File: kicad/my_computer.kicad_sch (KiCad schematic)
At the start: 15 parts, among them SW1 SW_SPST

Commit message: update schematic
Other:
- added sheet RAM (RAM.kicad_sch)
- moved on the sheet: R1
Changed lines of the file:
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@@
+	(wire
+		(pts
+			(xy 226.06 73.66) (xy 226.06 72.39)
+		)
+		(stroke
+			(width 0)
+			(type default)
+		)
+	)
 	(wire
 		(pts
@@
 	(wire
 		(pts
-			(xy 226.06 80.01) (xy 226.06 83.82)
+			(xy 226.06 81.28) (xy 226.06 83.82)
 		)
 		(stroke
@@
 	(symbol
 		(lib_id "Device:R")
-		(at 226.06 76.2 0)
+		(at 226.06 77.47 0)
 		(unit 1)
 		(exclude_from_sim no)
@@
 		(fields_autoplaced yes)
 		(property "Reference" "R1"
-			(at 228.6 74.9299 0)
+			(at 228.6 76.1999 0)
 			(effects
 				(font
@@
 		)
 		(property "Value" "10k"
-			(at 228.6 77.4699 0)
-			(effects
-				(font
-					(size 1.27 1.27)
-				)
-				(justify left)
-			)
-		)
-		(property "Footprint" ""
-			(at 224.282 76.2 90)
+			(at 228.6 78.7399 0)
+			(effects
+				(font
+					(size 1.27 1.27)
+				)
+				(justify left)
+			)
+		)
+		(property "Footprint" ""
+			(at 224.282 77.47 90)
 			(effects
 				(font
@@
 		)
 		(property "Datasheet" "~"
-			(at 226.06 76.2 0)
+			(at 226.06 77.47 0)
 			(effects
 				(font
@@
 		)
 		(property "Description" "Resistor"
-			(at 226.06 76.2 0)
+			(at 226.06 77.47 0)
 			(effects
 				(font
@@
 				)
 			)
+		)
+	)
+	(sheet
+		(at 554.99 86.36)
+		(size 224.79 147.32)
+		(exclude_from_sim no)
+		(in_bom yes)
+		(on_board yes)
+		(dnp no)
+		(fields_autoplaced yes)
+		(stroke
+			(width 0.1524)
+			(type solid)
+		)
+		(fill
+			(color 0 0 0 0.0000)
+		)
+		(property "Sheetname" "RAM"
+			(at 554.99 85.6484 0)
+			(effects
+				(font
+					(size 1.27 1.27)
+				)
+				(justify left bottom)
+			)
+		)
+		(property "Sheetfile" "RAM.kicad_sch"
+			(at 554.99 234.2646 0)
+			(effects
+				(font
+					(size 1.27 1.27)
+				)
+				(justify left top)
+			)
+		)
+		(instances
+			(project "my_computer"
+				(path "/d90612be-a4bb-4b59-8bc6-93e31ea1f515"
+					(page "4")
+				)
+			)

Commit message: update schematic
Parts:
- removed 555_TIMER: LMC555CMX_NOPB, LMC555CMX_NOPB:SOIC127P599X175-8N, symbol LMC555CMX_NOPB:LMC555CMX_NOPB
- removed C3: 0.01uF, symbol Device:C
- removed C4: 1uF, symbol Device:C
- added C11: 0.01uF, symbol Device:C
- added C12: 1uF, symbol Device:C
- added CLK: LMC555CMX_NOPB, LMC555CMX_NOPB:SOIC127P599X175-8N, symbol LMC555CMX_NOPB:LMC555CMX_NOPB
- added R11, R12, R13, R32, R4, R5, R6, R7, R8: 10k, symbol Device:R
- added R30: 1k, symbol Device:R
- added R31: 100k, symbol Device:R
- added SW10, SW11, SW12, SW13, SW14, SW2, SW3, SW4, SW5, SW6, SW9: SW_SPST, symbol Switch:SW_SPST
- R2: value 1k -> 10k
- R3: value 100k -> 10k
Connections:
- net +3.3V: now also R3.1, CLK.8 (V+), R11.1, R12.1, R13.1, R30.1, R32.1, R4.1, R5.1, R6.1, R7.1, R8.1
- net CLK_RST: now also CLK.4 (~{RESET})
- net GND: now also C11.1, C12.2, SW10.1 (A), SW11.1 (A), SW12.1 (A), SW13.1 (A), SW14.1 (A), SW2.1 (A), SW3.1 (A), SW4.1 (A), SW5.1 (A), SW6.1 (A), SW9.1 (A)
- net WE_RAM: now reaches R3.2
- net WE_RAM: now also SW13.2 (B)
- net CE_RAM: now reaches R2.2
- net CE_RAM: now also SW12.2 (B); no longer R3.1
- new net: CLK.7 (DISCHARGE), R30.2, R31.1
- new net: C12.1, CLK.2 (~{TRIGGER}), CLK.6 (THRESHOLD), R31.2
- new net: C11.2, CLK.5 (CONTROL_VOLTAGE)
- new net CLR: R13.2, SW11.2 (B)
- new net LD_A: R11.2, SW9.2 (B)
- new net LD_B: R8.2, SW6.2 (B)
- new net LD_X: R4.2, SW2.2 (B)
- new net LD_Y: R6.2, SW4.2 (B)
- new net OE_A: R12.2, SW10.2 (B)
- new net OE_RAM: R32.2, SW14.2 (B)
- new net OE_X: R5.2, SW3.2 (B)
- new net OE_Y: R7.2, SW5.2 (B)
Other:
- added sheet ALU_REGS (ALU_REGS.kicad_sch)
- moved on the sheet: R1, SW1

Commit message: add PC
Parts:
- added R10, R34, R9: 10k, symbol Device:R
- added SW15, SW7, SW8: SW_SPST, symbol Switch:SW_SPST
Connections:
- net +3.3V: now also R34.1, R9.1, SW8.2 (B)
- net GND: now also R10.2, SW15.1 (A), SW7.1 (A)
- new net CLR_PC: R10.1, SW8.1 (A)
- new net INC_PC: R34.2, SW15.2 (B)
- new net LD_PC: R9.2, SW7.2 (B)
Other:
- added sheet Control Unit (CTRL_UNIT.kicad_sch)

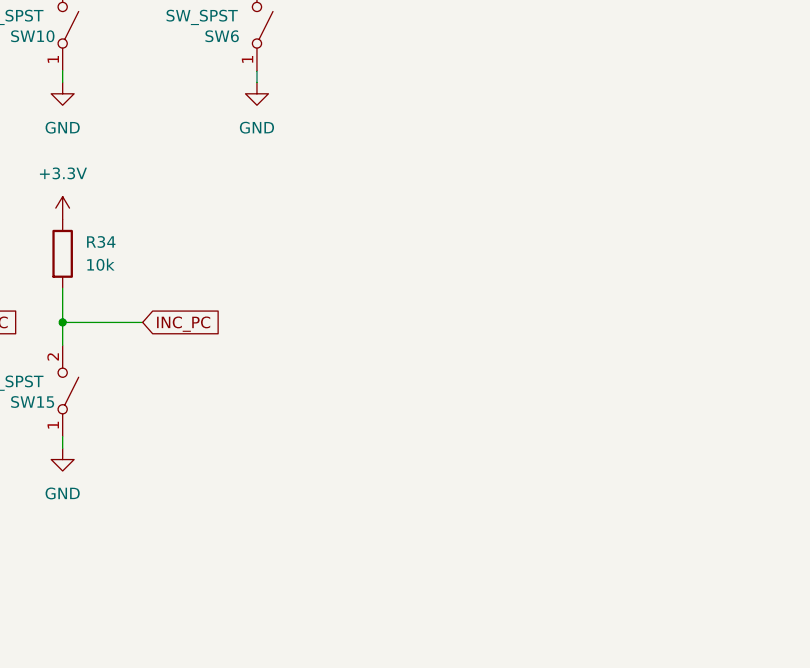
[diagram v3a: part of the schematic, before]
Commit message: update schematic
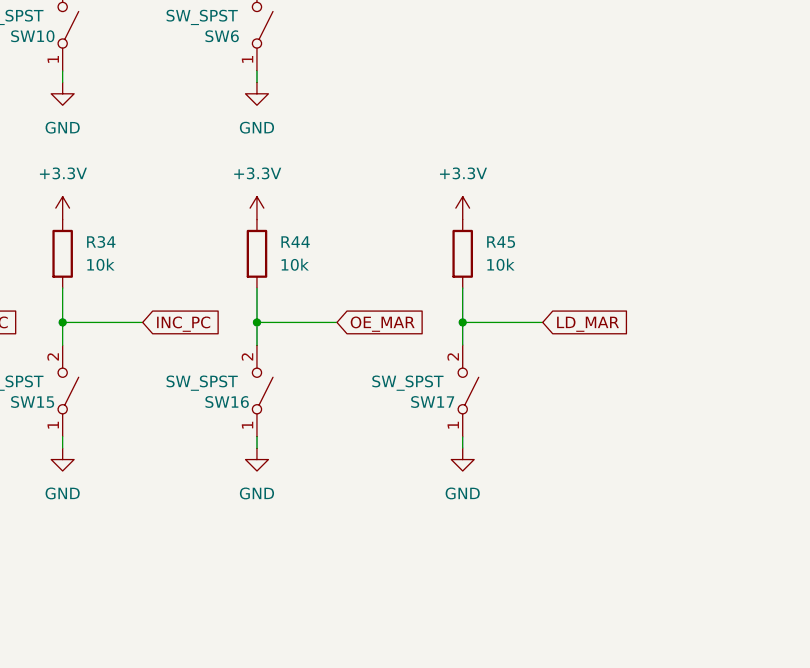
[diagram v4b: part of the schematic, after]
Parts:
- added R44, R45: 10k, symbol Device:R
- added SW16, SW17: SW_SPST, symbol Switch:SW_SPST
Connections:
- net +3.3V: now also R44.1, R45.1
- net GND: now also SW16.1 (A), SW17.1 (A)
- new net LD_MAR: R45.2, SW17.2 (B)
- new net OE_MAR: R44.2, SW16.2 (B)

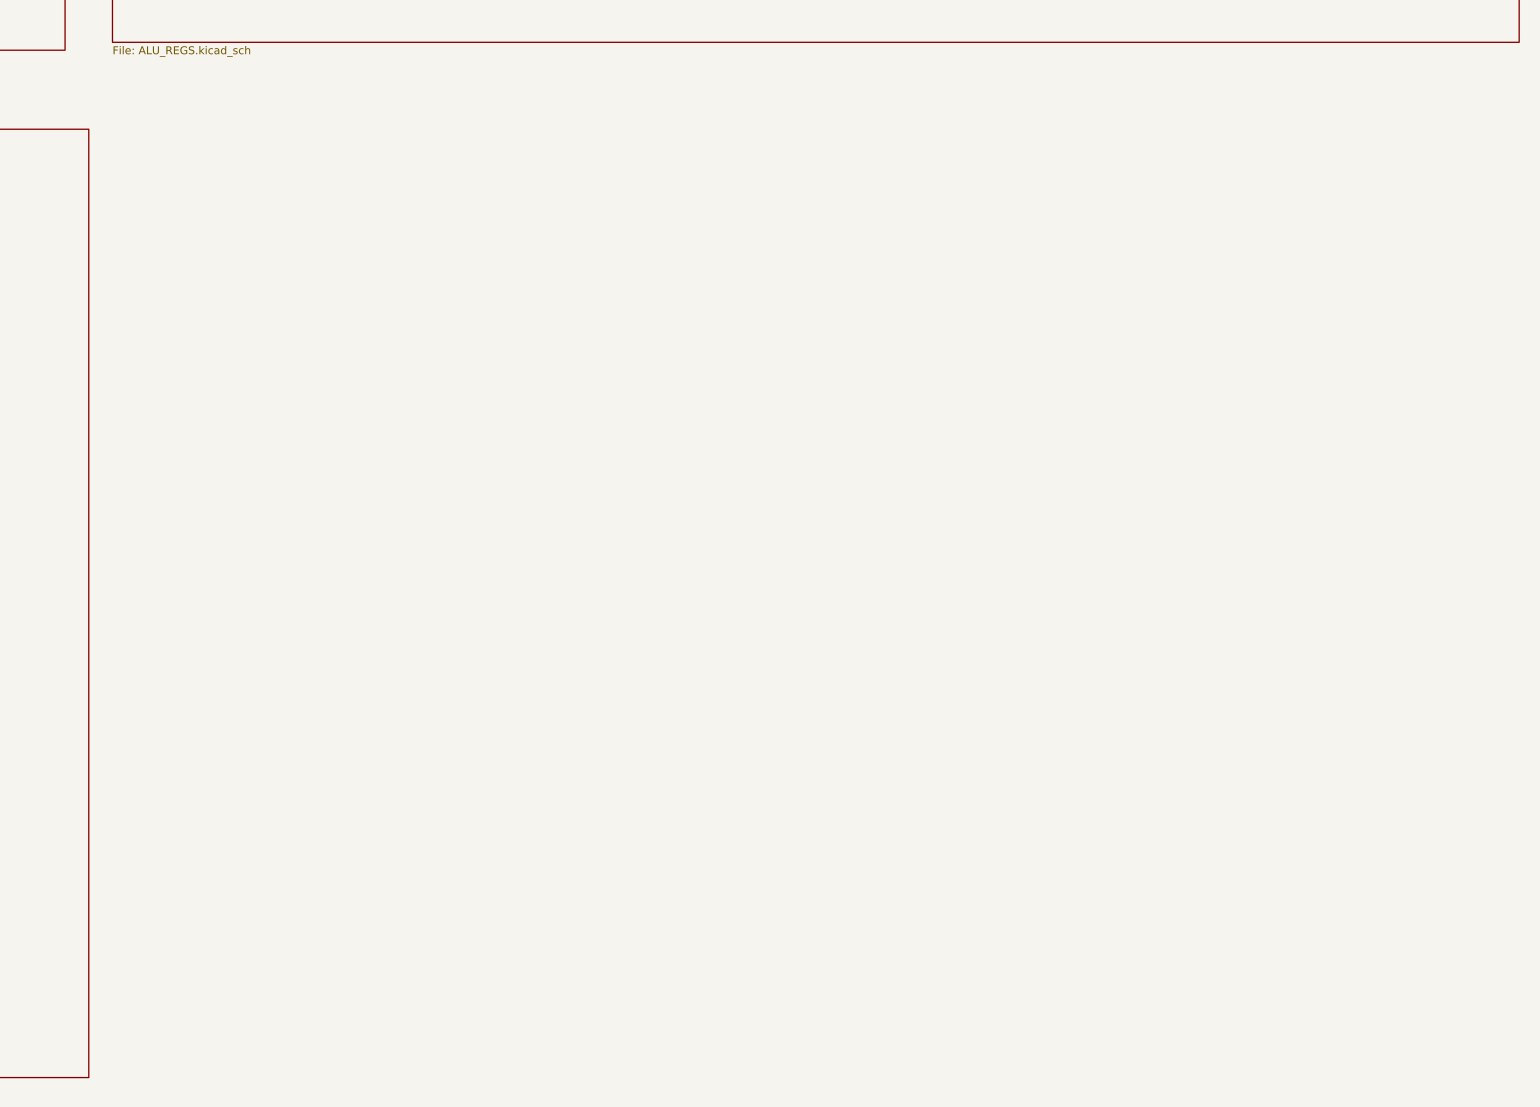
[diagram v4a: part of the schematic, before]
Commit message: add instruction decoder
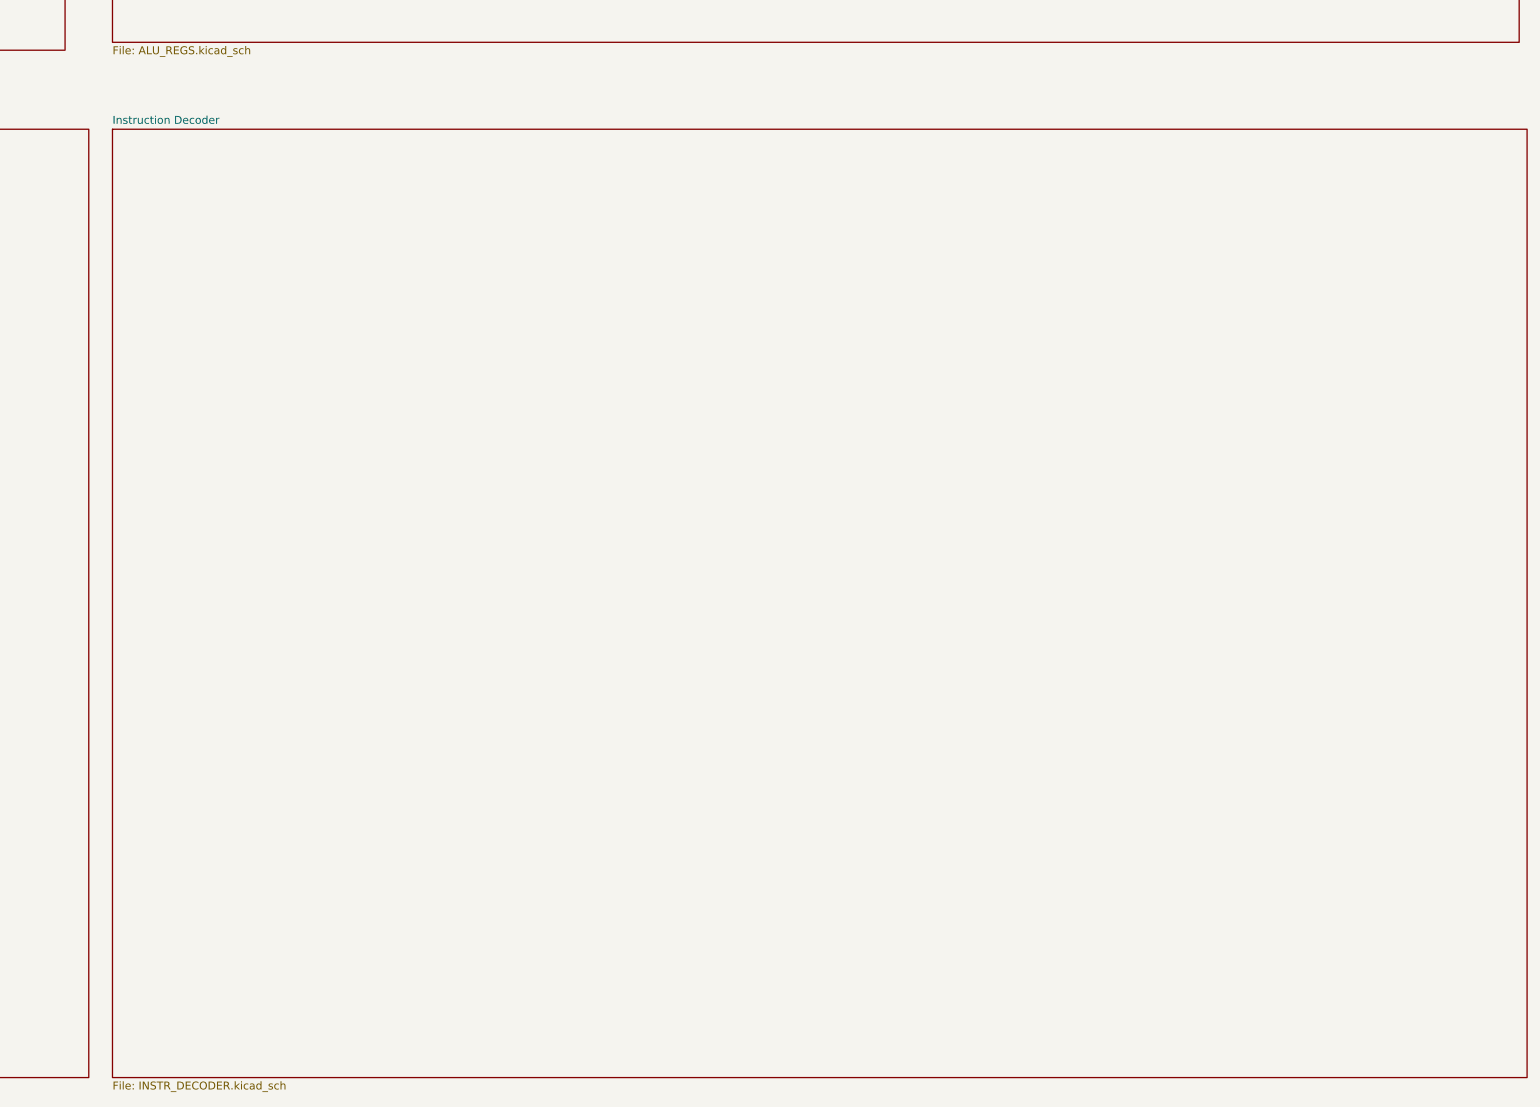
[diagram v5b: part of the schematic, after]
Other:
- added sheet Instruction Decoder (INSTR_DECODER.kicad_sch)
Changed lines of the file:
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@@
+		)
+	)
+	(sheet
+		(at 572.77 260.35)
+		(size 227.33 152.4)
+		(exclude_from_sim no)
+		(in_bom yes)
+		(on_board yes)
+		(dnp no)
+		(fields_autoplaced yes)
+		(stroke
+			(width 0.1524)
+			(type solid)
+		)
+		(fill
+			(color 0 0 0 0.0000)
+		)
+		(property "Sheetname" "Instruction Decoder"
+			(at 572.77 259.6384 0)
+			(effects
+				(font
+					(size 1.27 1.27)
+				)
+				(justify left bottom)
+			)
+		)
+		(property "Sheetfile" "INSTR_DECODER.kicad_sch"
+			(at 572.77 413.3346 0)
+			(effects
+				(font
+					(size 1.27 1.27)
+				)
+				(justify left top)
+			)
+		)
+		(instances
+			(project "my_computer"
+				(path "/d90612be-a4bb-4b59-8bc6-93e31ea1f515"
+					(page "7")
+				)
+			)
 		)
 	)
